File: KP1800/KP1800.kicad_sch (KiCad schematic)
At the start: 19 parts, among them J1 USB_C_Receptacle_USB2.0_14P, SW1 SW_Push, SW2 SW_Push, U1 USBLC6-2SC6, U2 STM32F072CBTx, U3 XC6206PxxxMR

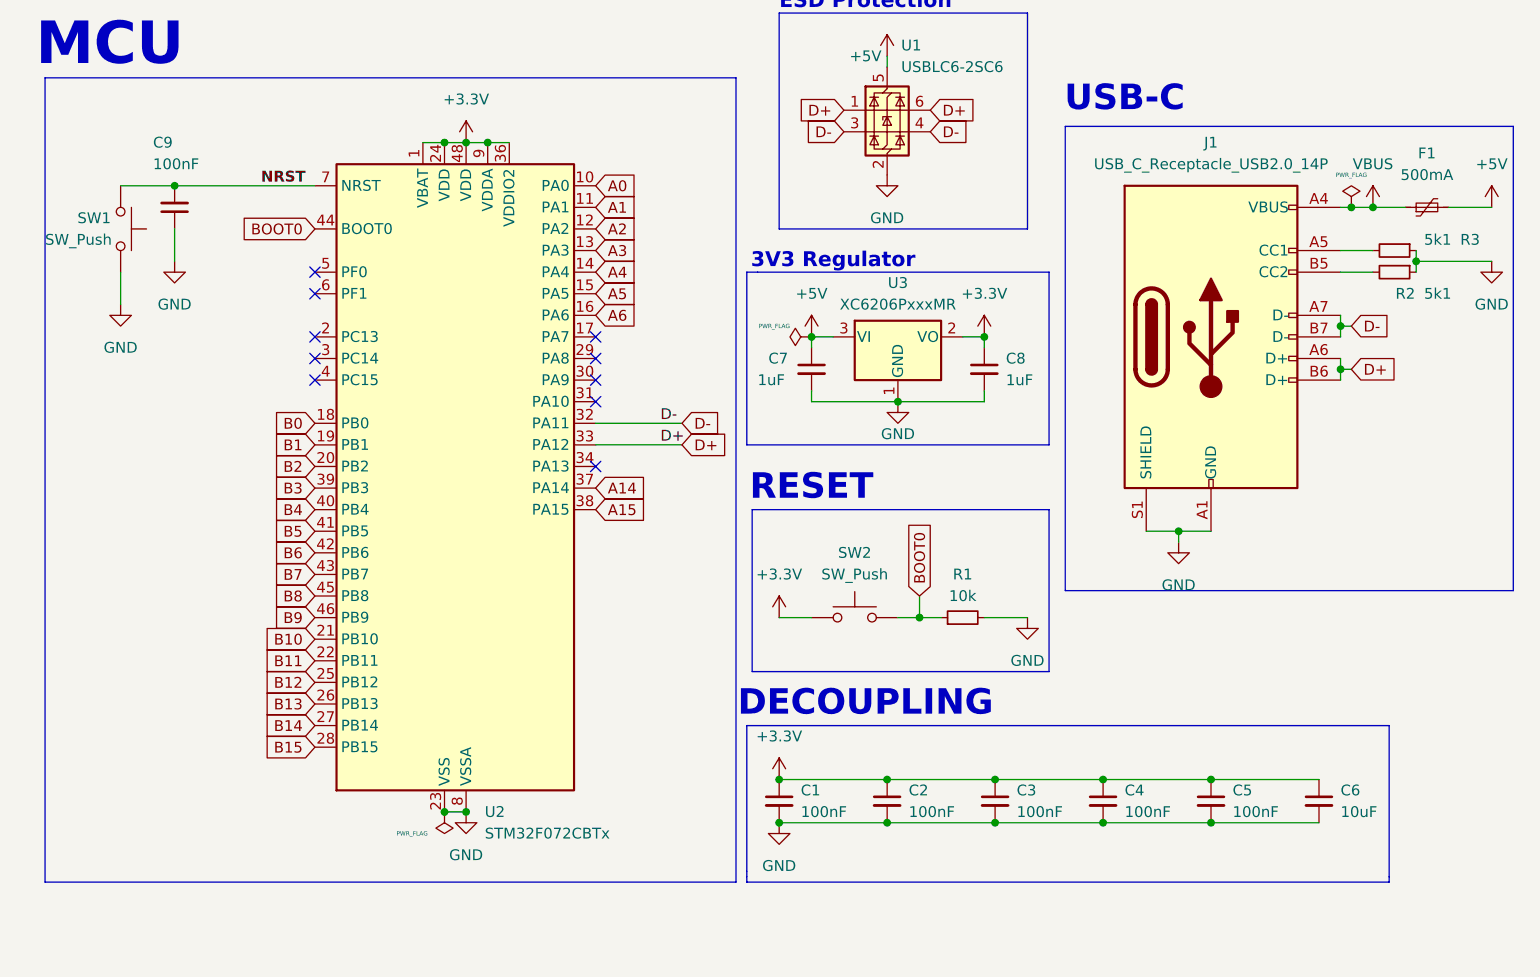
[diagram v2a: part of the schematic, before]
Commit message: Working on PCB // Laid out key switches // 60% board
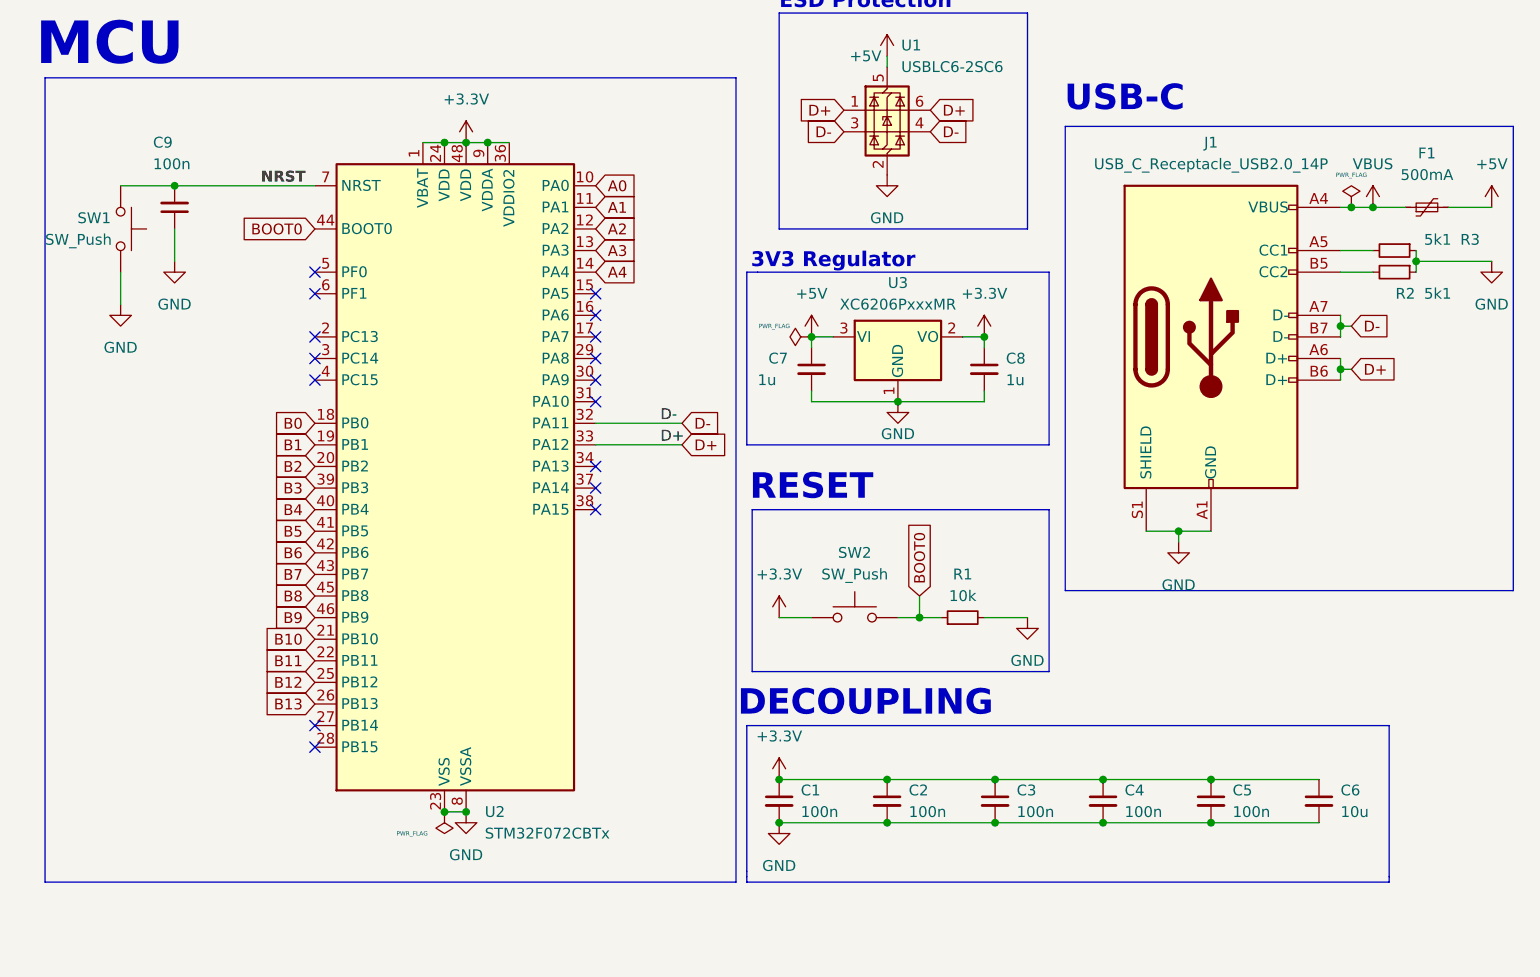
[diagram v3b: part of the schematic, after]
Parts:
- C1, C2, C3, C4, C5, C9: value 100nF -> 100n; footprint (none) -> Capacitor_SMD:C_0805_2012Metric_Pad1.18x1.45mm_HandSolder
- C6: value 10uF -> 10u; footprint (none) -> Capacitor_SMD:C_0805_2012Metric_Pad1.18x1.45mm_HandSolder
- C7, C8: value 1uF -> 1u; footprint (none) -> Capacitor_SMD:C_0805_2012Metric_Pad1.18x1.45mm_HandSolder
- F1: footprint (none) -> Fuse:Fuse_1206_3216Metric_Pad1.42x1.75mm_HandSolder
- J1: footprint (none) -> Connector_USB:USB_C_Receptacle_HRO_TYPE-C-31-M-12
- R1, R2, R3: footprint (none) -> Resistor_SMD:R_0805_2012Metric_Pad1.20x1.40mm_HandSolder
- SW1, SW2: footprint (none) -> Button_Switch_SMD:SW_SPST_TL3342
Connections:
- net A14: no longer names the net of U2.37 (PA14)
- net A15: no longer names the net of U2.38 (PA15)
- net A5: no longer names the net of U2.15 (PA5)
- net A6: no longer names the net of U2.16 (PA6)
- net B14: no longer names the net of U2.27 (PB14)
- net B15: no longer names the net of U2.28 (PB15)
- no-connect marks 10 -> 16
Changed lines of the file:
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@@
 	)
 	(no_connect
+		(at 83.82 125.73)
+	)
+	(no_connect
 		(at 83.82 77.47)
 	)
@@
 	)
 	(no_connect
+		(at 83.82 123.19)
+	)
+	(no_connect
+		(at 116.84 95.25)
+	)
+	(no_connect
+		(at 116.84 97.79)
+	)
+	(no_connect
+		(at 116.84 72.39)
+	)
+	(no_connect
 		(at 116.84 92.71)
 	)
 	(no_connect
+		(at 116.84 74.93)
+	)
+	(no_connect
 		(at 116.84 85.09)
 	)
@@
 		)
 	)
-	(global_label "A15"
-		(shape input)
-		(at 116.84 97.79 0)
-		(fields_autoplaced yes)
-		(effects
-			(font
-				(size 1.27 1.27)
-			)
-			(justify left)
-		)
-		(property "Intersheetrefs" "${INTERSHEET_REFS}"
-			(at 123.3328 97.79 0)
-			(effects
-				(font
-					(size 1.27 1.27)
-				)
-				(justify left)
-				(hide yes)
-			)
-		)
-	)
 	(global_label "B5"
 		(shape input)
@@
 		)
 	)
-	(global_label "A5"
-		(shape input)
-		(at 116.84 72.39 0)
-		(fields_autoplaced yes)
-		(effects
-			(font
-				(size 1.27 1.27)
-			)
-			(justify left)
-		)
-		(property "Intersheetrefs" "${INTERSHEET_REFS}"
-			(at 122.1233 72.39 0)
-			(effects
-				(font
-					(size 1.27 1.27)
-				)
-				(justify left)
-				(hide yes)
-			)
-		)
-	)
 	(global_label "D-"
 		(shape input)
@@
 		)
 	)
-	(global_label "A6"
-		(shape input)
-		(at 116.84 74.93 0)
-		(fields_autoplaced yes)
-		(effects
-			(font
-				(size 1.27 1.27)
-			)
-			(justify left)
-		)
-		(property "Intersheetrefs" "${INTERSHEET_REFS}"
-			(at 122.1233 74.93 0)
-			(effects
-				(font
-					(size 1.27 1.27)
-				)
-				(justify left)
-				(hide yes)
-			)
-		)
-	)
 	(global_label "BOOT0"
 		(shape input)
@@
 		)
 	)
-	(global_label "B14"
-		(shape input)
-		(at 83.82 123.19 180)
-		(fields_autoplaced yes)
-		(effects
-			(font
-				(size 1.27 1.27)
-			)
-			(justify right)
-		)
-		(property "Intersheetrefs" "${INTERSHEET_REFS}"
-			(at 77.1458 123.19 0)
-			(effects
-				(font
-					(size 1.27 1.27)
-				)
-				(justify right)
-				(hide yes)
-			)
-		)
-	)
 	(global_label "B7"
 		(shape input)
@@
 		)
 	)
-	(global_label "B15"
-		(shape input)
-		(at 83.82 125.73 180)
-		(fields_autoplaced yes)
-		(effects
-			(font
-				(size 1.27 1.27)
-			)
-			(justify right)
-		)
-		(property "Intersheetrefs" "${INTERSHEET_REFS}"
-			(at 77.1458 125.73 0)
-			(effects
-				(font
-					(size 1.27 1.27)
-				)
-				(justify right)
-				(hide yes)
-			)
-		)
-	)
-	(global_label "A14"
-		(shape input)
-		(at 116.84 95.25 0)
-		(fields_autoplaced yes)
-		(effects
-			(font
-				(size 1.27 1.27)
-			)
-			(justify left)
-		)
-		(property "Intersheetrefs" "${INTERSHEET_REFS}"
-			(at 123.3328 95.25 0)
-			(effects
-				(font
-					(size 1.27 1.27)
-				)
-				(justify left)
-				(hide yes)
-			)
-		)
-	)
 	(symbol
 		(lib_id "Device:Polyfuse_Small")
@@
 			)
 		)
-		(property "Footprint" ""
+		(property "Footprint" "Fuse:Fuse_1206_3216Metric_Pad1.42x1.75mm_HandSolder"
 			(at 219.71 60.96 0)
 			(effects
@@
 			)
 		)
-		(property "Value" "100nF"
+		(property "Value" "100n"
 			(at 166.37 133.3562 0)
 			(effects
@@
 			)
 		)
-		(property "Footprint" ""
+		(property "Footprint" "Capacitor_SMD:C_0805_2012Metric_Pad1.18x1.45mm_HandSolder"
 			(at 163.83 132.08 0)
 			(effects
@@
 			)
 		)
-		(property "Value" "100nF"
+		(property "Value" "100n"
 			(at 140.97 133.3562 0)
 			(effects
@@
 			)
 		)
-		(property "Footprint" ""
+		(property "Footprint" "Capacitor_SMD:C_0805_2012Metric_Pad1.18x1.45mm_HandSolder"
 			(at 138.43 132.08 0)
 			(effects
@@
 			)
 		)
-		(property "Value" "1uF"
+		(property "Value" "1u"
 			(at 135.89 82.55 0)
 			(effects
@@
 			)
 		)
-		(property "Footprint" ""
+		(property "Footprint" "Capacitor_SMD:C_0805_2012Metric_Pad1.18x1.45mm_HandSolder"
 			(at 142.24 81.28 0)
 			(effects
@@
 			)
 		)
-		(property "Footprint" ""
+		(property "Footprint" "Connector_USB:USB_C_Receptacle_HRO_TYPE-C-31-M-12"
 			(at 193.04 77.47 0)
 			(effects
@@
 			)
 		)
-		(property "Value" "10uF"
+		(property "Value" "10u"
 			(at 204.47 133.3562 0)
 			(effects
@@
 			)
 		)
-		(property "Footprint" ""
+		(property "Footprint" "Capacitor_SMD:C_0805_2012Metric_Pad1.18x1.45mm_HandSolder"
 			(at 201.93 132.08 0)
 			(effects
@@
 			)
 		)
-		(property "Value" "100nF"
+		(property "Value" "100n"
 			(at 191.77 133.3562 0)
 			(effects
@@
 			)
 		)
-		(property "Footprint" ""
+		(property "Footprint" "Capacitor_SMD:C_0805_2012Metric_Pad1.18x1.45mm_HandSolder"
 			(at 189.23 132.08 0)
 			(effects
@@
 			)
 		)
-		(property "Footprint" ""
+		(property "Footprint" "Button_Switch_SMD:SW_SPST_TL3342"
 			(at 66.04 64.77 0)
 			(effects
@@
 			)
 		)
-		(property "Footprint" ""
+		(property "Footprint" "Button_Switch_SMD:SW_SPST_TL3342"
 			(at 147.32 105.41 0)
 			(effects
@@
 			)
 		)
-		(property "Footprint" ""
+		(property "Footprint" "Resistor_SMD:R_0805_2012Metric_Pad1.20x1.40mm_HandSolder"
 			(at 210.82 69.85 0)
 			(effects
@@
 			)
 		)
-		(property "Value" "100nF"
+		(property "Value" "100n"
 			(at 179.07 133.3562 0)
 			(effects
@@
 			)
 		)
-		(property "Footprint" ""
+		(property "Footprint" "Capacitor_SMD:C_0805_2012Metric_Pad1.18x1.45mm_HandSolder"
 			(at 176.53 132.08 0)
 			(effects
@@
 			)
 		)
-		(property "Footprint" ""
+		(property "Footprint" "Resistor_SMD:R_0805_2012Metric_Pad1.20x1.40mm_HandSolder"
 			(at 210.82 67.31 0)
 			(effects
@@
 			)
 		)
-		(property "Value" "1uF"
+		(property "Value" "1u"
 			(at 165.1 82.5562 0)
 			(effects
@@
 			)
 		)
-		(property "Footprint" ""
+		(property "Footprint" "Capacitor_SMD:C_0805_2012Metric_Pad1.18x1.45mm_HandSolder"
 			(at 162.56 81.28 0)
 			(effects
@@
 			)
 		)
-		(property "Footprint" ""
+		(property "Footprint" "Resistor_SMD:R_0805_2012Metric_Pad1.20x1.40mm_HandSolder"
 			(at 160.02 110.49 0)
 			(effects
@@
 			)
 		)
-		(property "Value" "100nF"
+		(property "Value" "100n"
 			(at 153.67 133.3562 0)
 			(effects
@@
 			)
 		)
-		(property "Footprint" ""
+		(property "Footprint" "Capacitor_SMD:C_0805_2012Metric_Pad1.18x1.45mm_HandSolder"
 			(at 151.13 132.08 0)
 			(effects
@@
 			)
 		)
-		(property "Value" "100nF"
+		(property "Value" "100n"
 			(at 64.77 57.15 0)
 			(effects
@@
 			)
 		)
-		(property "Footprint" ""
+		(property "Footprint" "Capacitor_SMD:C_0805_2012Metric_Pad1.18x1.45mm_HandSolder"
 			(at 67.31 62.23 0)
 			(effects

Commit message: Added traces to matrix
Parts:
- R1, R2, R3: footprint Resistor_SMD:R_0805_2012Metric_Pad1.20x1.40mm_HandSolder -> Resistor_SMD:R_0603_1608Metric_Pad0.98x0.95mm_HandSolder
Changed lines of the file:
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@@
 			)
 		)
-		(property "Footprint" "Resistor_SMD:R_0805_2012Metric_Pad1.20x1.40mm_HandSolder"
+		(property "Footprint" "Resistor_SMD:R_0603_1608Metric_Pad0.98x0.95mm_HandSolder"
 			(at 210.82 69.85 0)
 			(effects
@@
 			)
 		)
-		(property "Footprint" "Resistor_SMD:R_0805_2012Metric_Pad1.20x1.40mm_HandSolder"
+		(property "Footprint" "Resistor_SMD:R_0603_1608Metric_Pad0.98x0.95mm_HandSolder"
 			(at 210.82 67.31 0)
 			(effects
@@
 			)
 		)
-		(property "Footprint" "Resistor_SMD:R_0805_2012Metric_Pad1.20x1.40mm_HandSolder"
+		(property "Footprint" "Resistor_SMD:R_0603_1608Metric_Pad0.98x0.95mm_HandSolder"
 			(at 160.02 110.49 0)
 			(effects

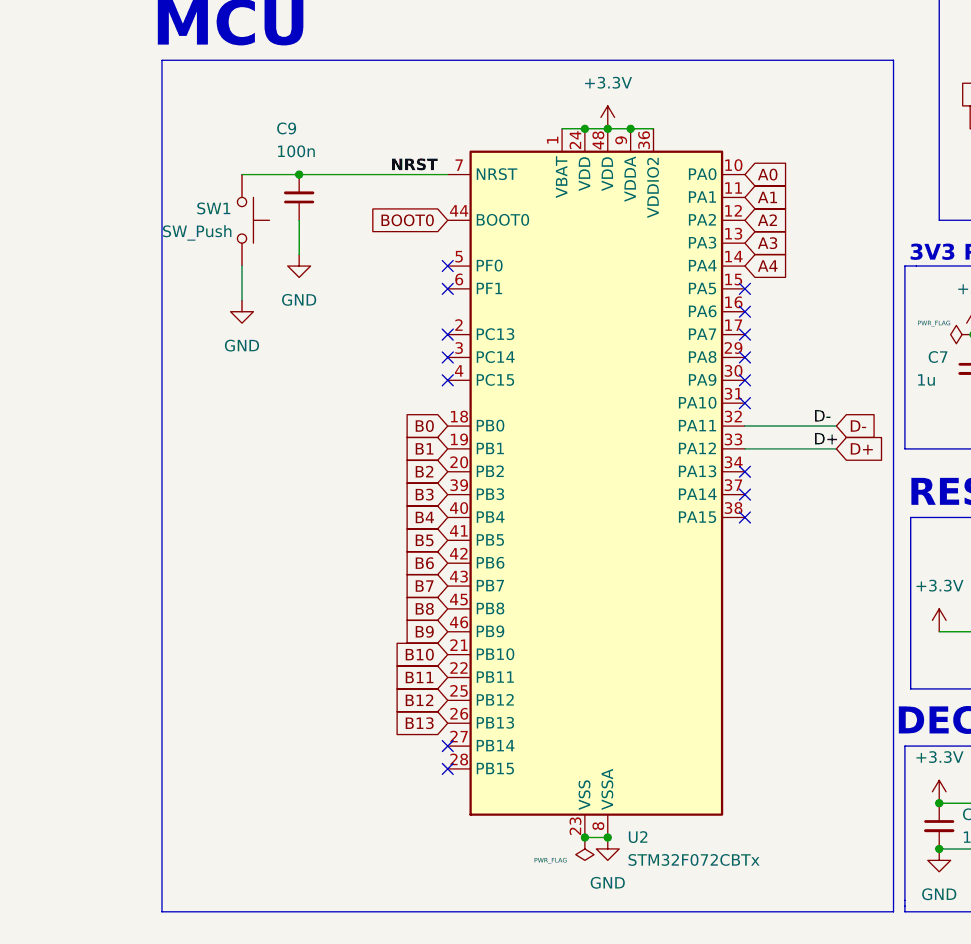
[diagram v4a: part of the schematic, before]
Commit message: All traces done. Now working on grounding.
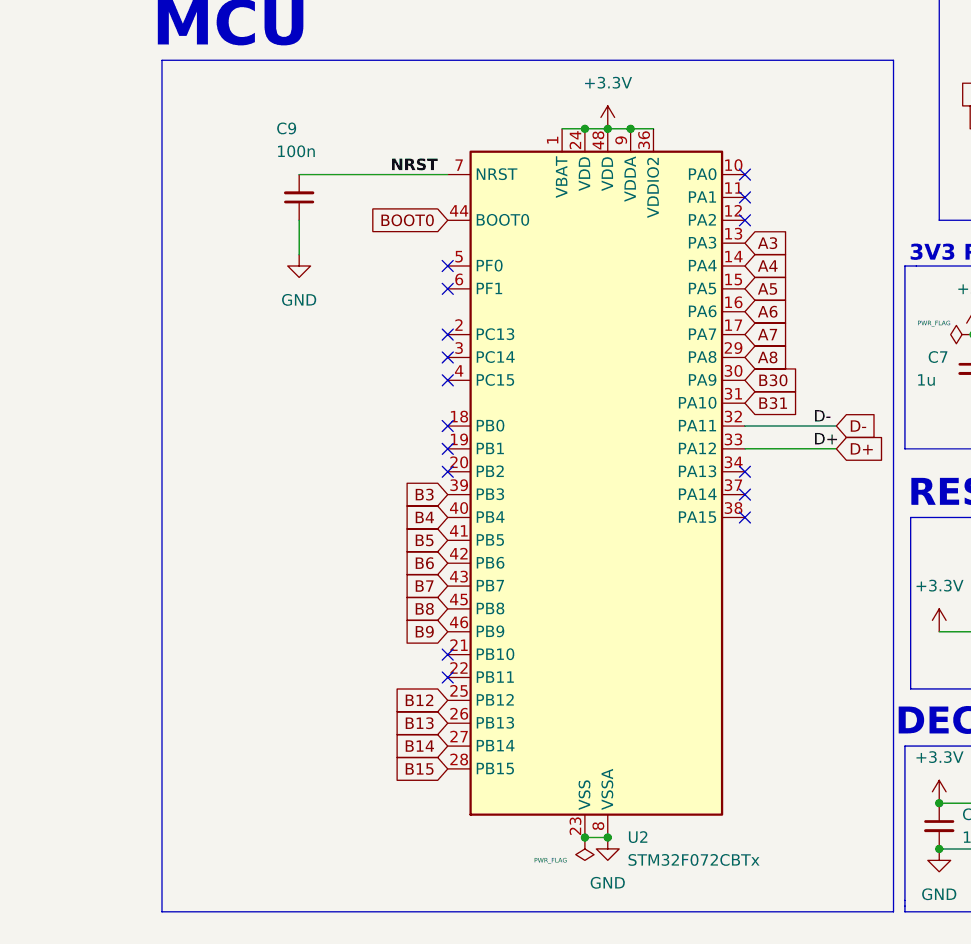
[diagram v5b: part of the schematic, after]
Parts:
- removed SW1: SW_Push, Button_Switch_SMD:SW_SPST_TL3342, symbol Switch:SW_Push
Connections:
- net A5: now reaches U2.15 (PA5)
- net A6: now reaches U2.16 (PA6)
- net A7: now reaches U2.17 (PA7)
- net B14: now reaches U2.27 (PB14)
- net B15: now reaches U2.28 (PB15)
- net A8: now reaches U2.29 (PA8)
- net B30: now reaches U2.30 (PA9)
- net B31: now reaches U2.31 (PA10)
- net A0: no longer names the net of U2.10 (PA0)
- net A1: no longer names the net of U2.11 (PA1)
- net A2: no longer names the net of U2.12 (PA2)
- net B0: no longer names the net of U2.18 (PB0)
- net B1: no longer names the net of U2.19 (PB1)
- net B10: no longer names the net of U2.21 (PB10)
- net B11: no longer names the net of U2.22 (PB11)
- net B2: no longer names the net of U2.20 (PB2)
